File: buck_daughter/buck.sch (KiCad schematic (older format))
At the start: 21 parts, among them P1 Modular Jack In, U1 LD1117, U2 AP73333, U3 ST485E, U4 TPS54360DDAR

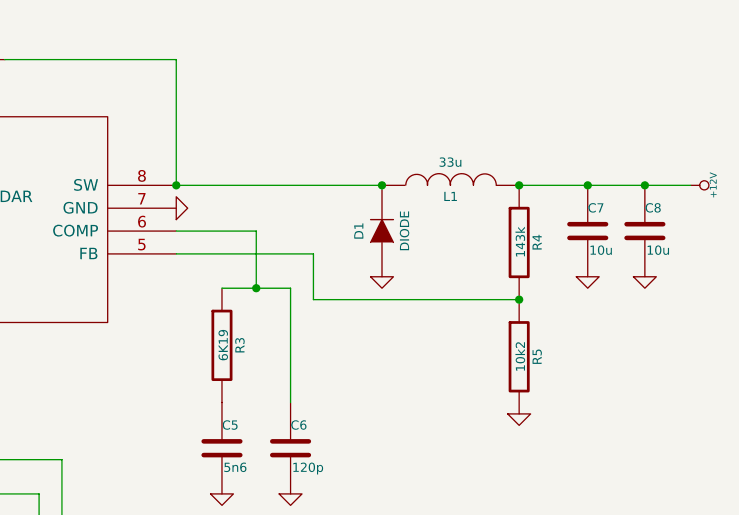
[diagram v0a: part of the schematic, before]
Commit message: Finished silkscreen on daughter board, it and digital led board are done\!
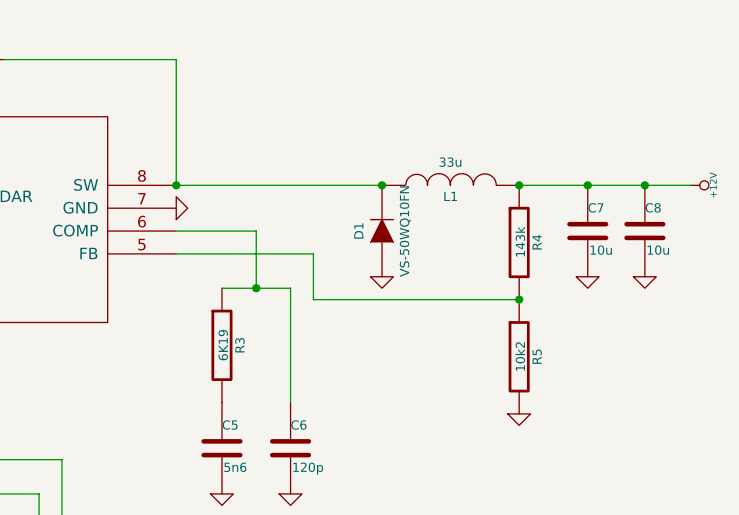
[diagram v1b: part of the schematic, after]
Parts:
- D1: value DIODE -> VS-50WQ10FN
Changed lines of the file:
@@
 Sheet 1 1
 Title ""
-Date "6 jan 2014"
+Date "9 jan 2014"
 Rev ""
 Comp ""
@@
 P 7000 1750
 F 0 "D1" H 7000 1850 40  0000 C CNN
-F 1 "DIODE" H 7000 1650 40  0000 C CNN
+F 1 "VS-50WQ10FN" H 7000 1650 40  0000 C CNN
 F 2 "" H 7000 1750 60  0000 C CNN
 F 3 "" H 7000 1750 60  0000 C CNN
